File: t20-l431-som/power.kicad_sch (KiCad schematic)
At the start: 40 parts, among them U1 STM32L431-WLCSP64, U2 T20W80, U4 MODULE_INTERNAL_T20_L431_HOST, U5 LP3986TL-2518/NOPB, U7 TPS22916BYFPR, U9 NCP139AFCT120T2G

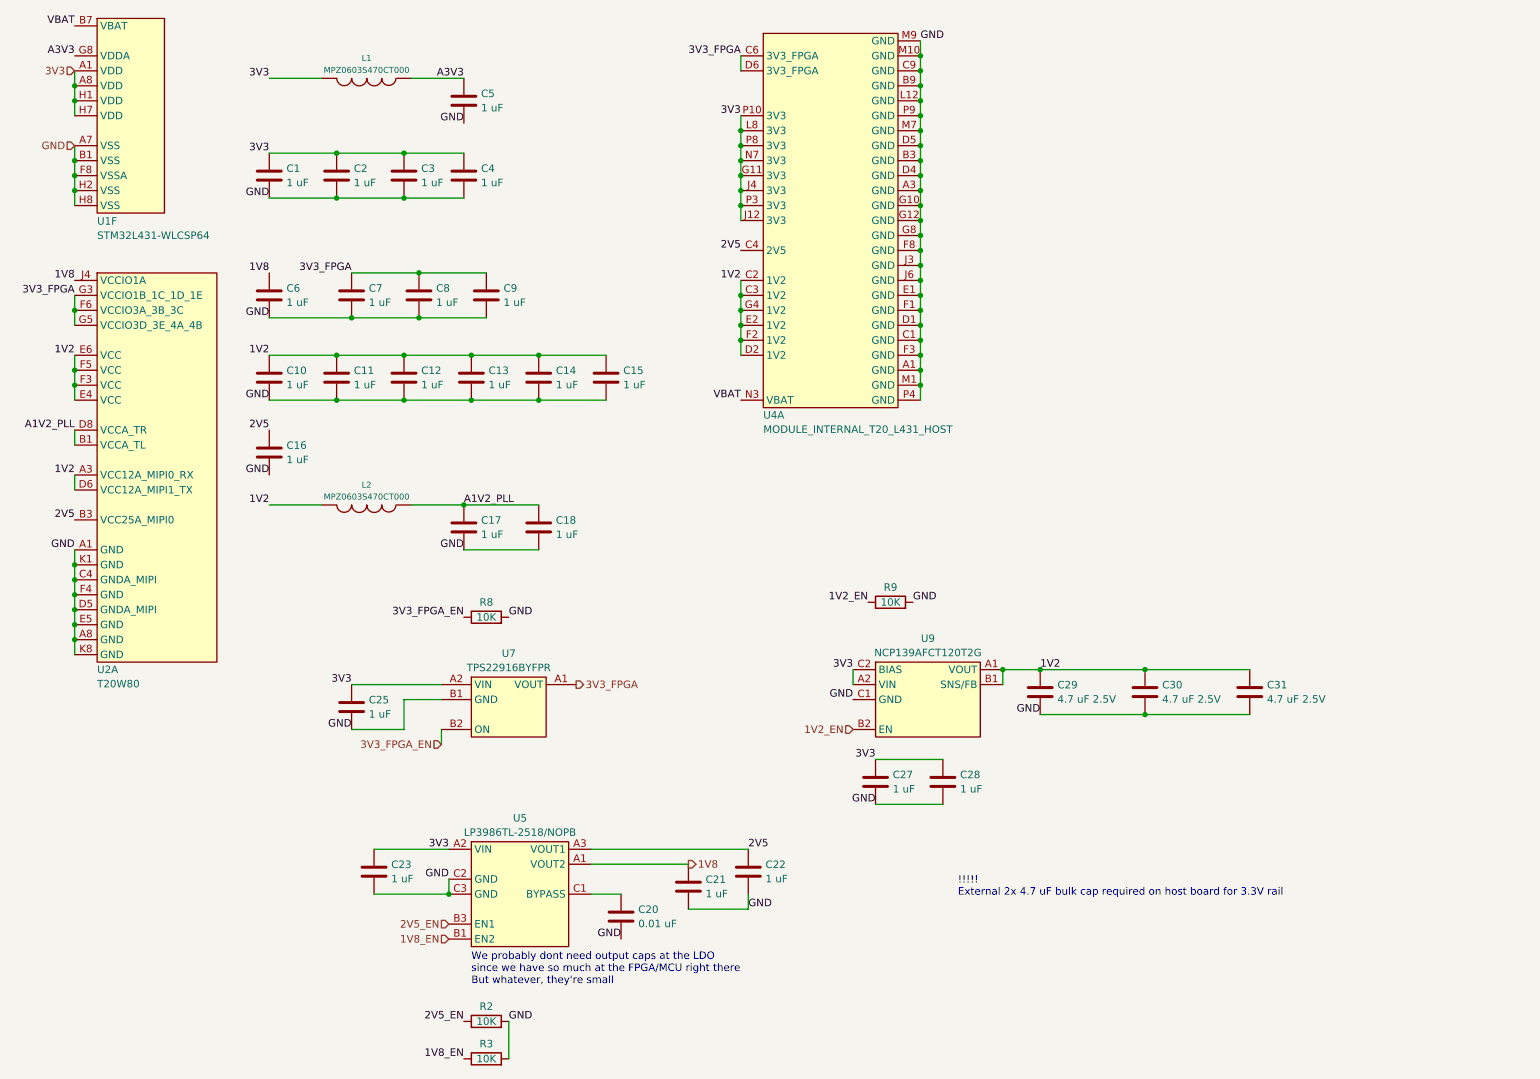
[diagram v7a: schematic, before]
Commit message: More work on T20-L431 module
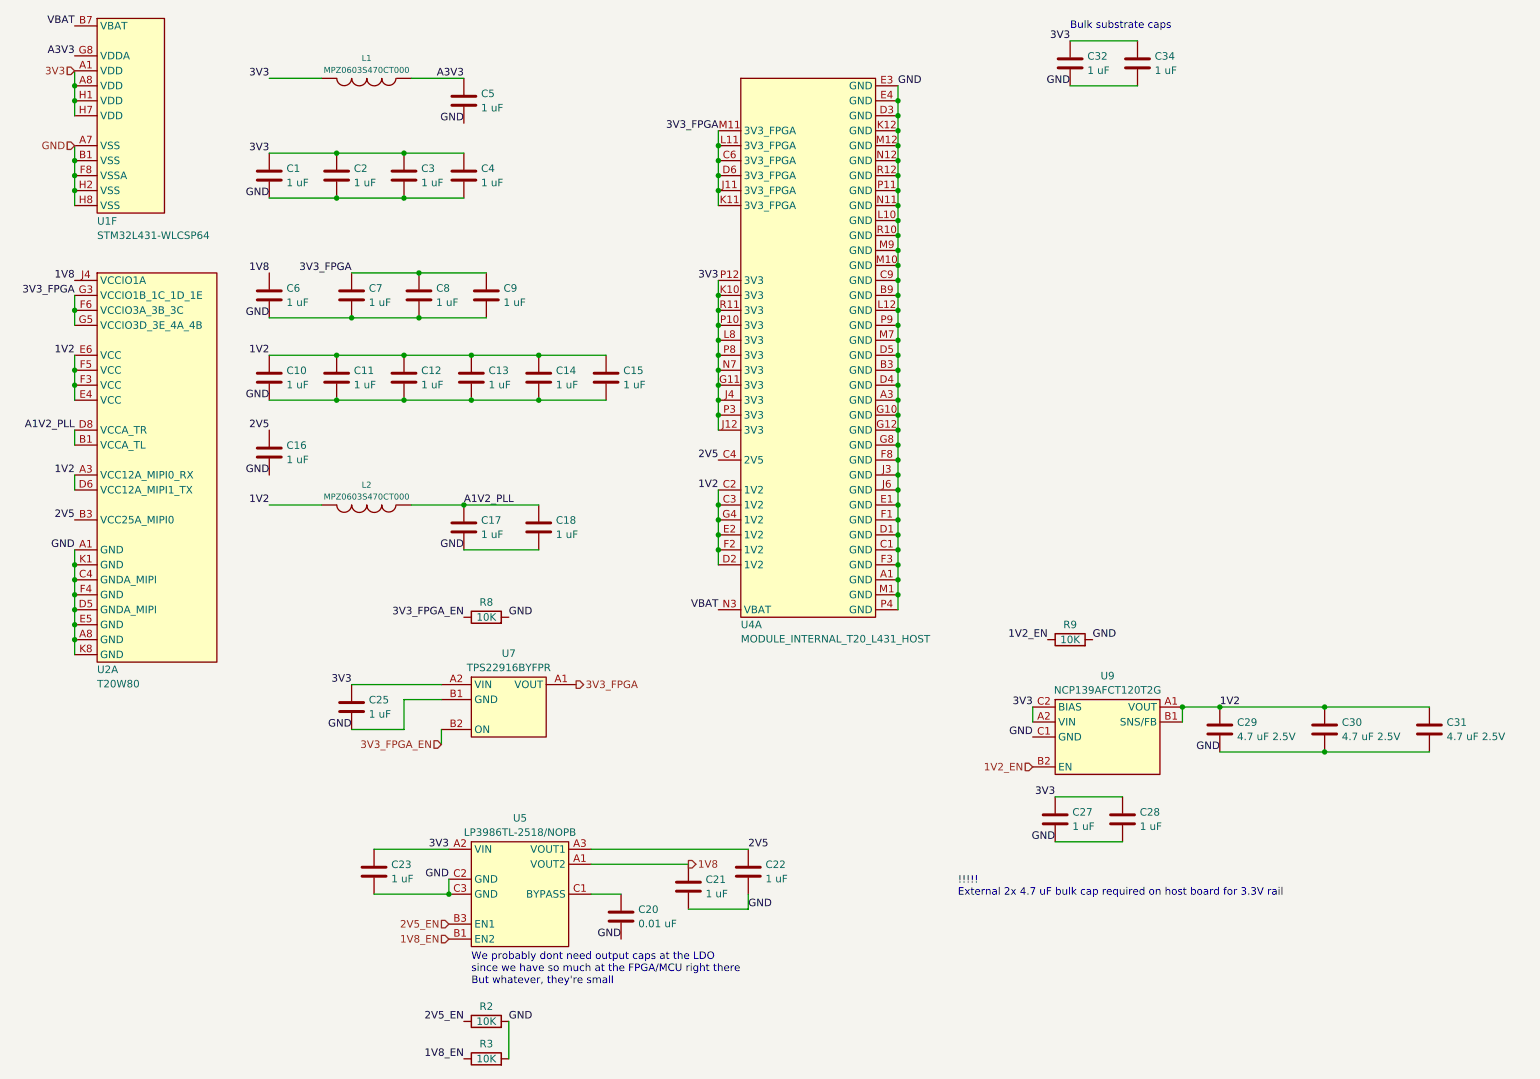
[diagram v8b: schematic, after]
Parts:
- added C32, C34: 1 uF, azonenberg_pcb:EIA_0201_CAP_NOSILK, symbol device:C
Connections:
- net 3V3: now also U4.K10 (3V3), U4.P12 (3V3), U4.R11 (3V3), C32.1, C34.1
- net 3V3_FPGA: now also U4.J11 (3V3_FPGA), U4.K11 (3V3_FPGA), U4.L11 (3V3_FPGA), U4.M11 (3V3_FPGA)
- net GND: now also U4.D3 (GND), U4.E3 (GND), U4.E4 (GND), U4.K12 (GND), U4.L10 (GND), U4.M12 (GND), U4.N11 (GND), U4.N12 (GND), U4.P11 (GND), U4.R10 (GND), U4.R12 (GND), C32.2, C34.2
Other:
- note added: "Bulk substrate caps"
- moved on the sheet: C27, C28, C29, C30, C31, R9, U9
